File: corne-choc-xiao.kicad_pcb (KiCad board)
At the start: 2 copper layers, 111.3 x 87.7 mm, 51 parts, among them J1 LiPo, Q1 SI2032, SW10 SW_PUSH, SW11 SW_PUSH, SW12 SW_PUSH, SW14 SW_PUSH, SW15 SW_PUSH, SW16 SW_PUSH, SW17 SW_PUSH, SW18 SW_PUSH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

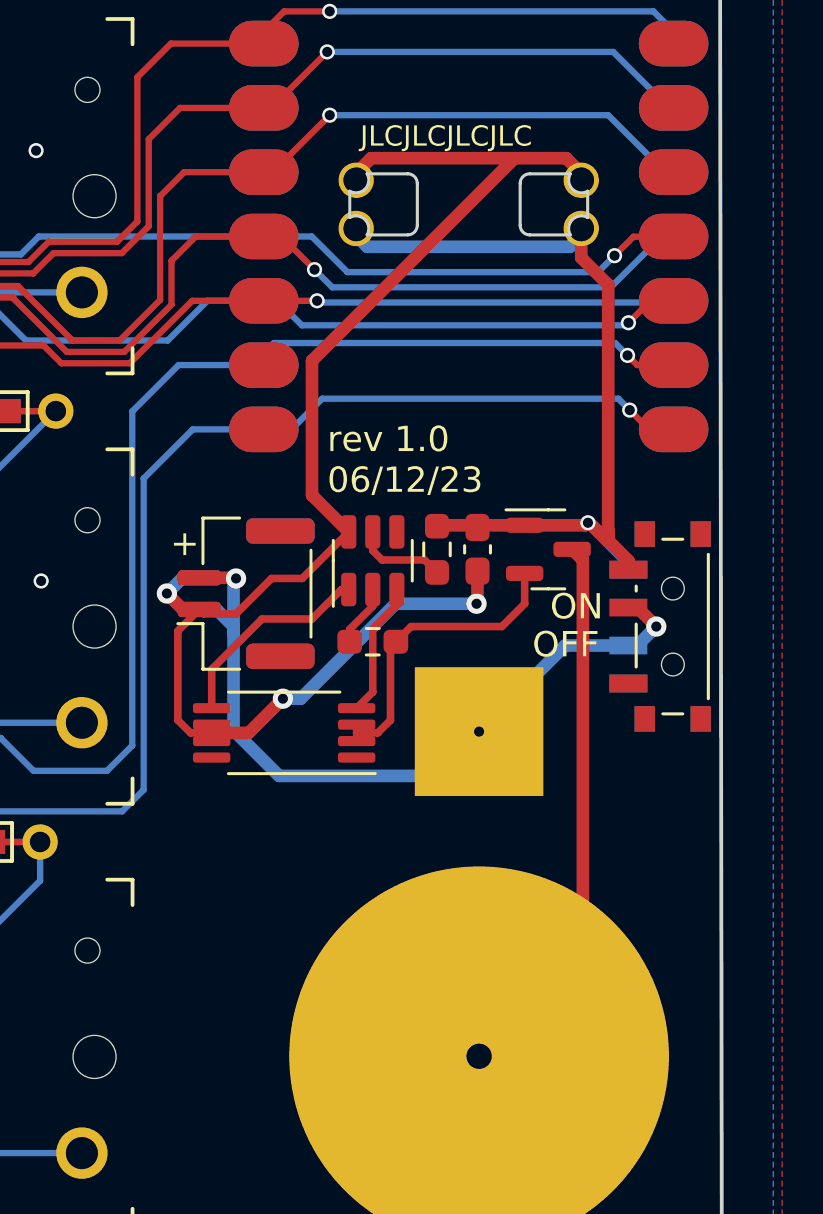
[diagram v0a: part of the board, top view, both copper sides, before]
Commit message: fix battery protection circuit
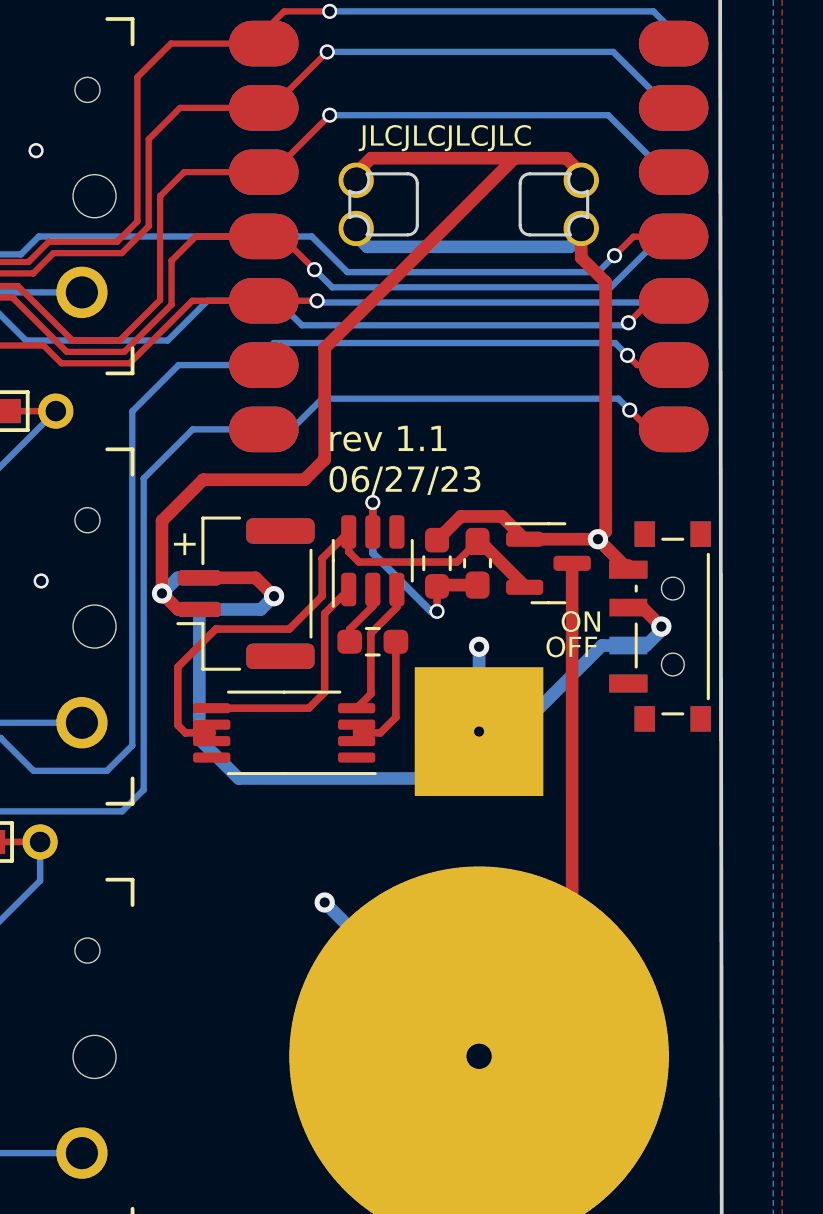
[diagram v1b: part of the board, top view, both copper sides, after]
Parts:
- BT1: value 3002 -> LIR2032
- Q1: value SI2032 -> SI2302
- R1: value 100R -> 330R
- R2: value 1k -> 2.7k
- moved C1 0.55 mm to (178.5, 75.9), turned to 90 degrees
- moved Q1 0.55 mm to (181.3, 75.9)
- moved R1 0.55 mm to (176.9, 75.9)
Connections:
- C1 pad 1: BAT+ -> Net-(U2-VCC)
- C1 pad 2: GND -> BAT-
- R2 pad 2: BAT- -> GND
- U2 pad 6: GND -> BAT-
- U3 pad 2: BAT- -> GND
- U3 pad 3: BAT- -> GND
- U3 pad 6: GND -> BAT-
- U3 pad 7: GND -> BAT-
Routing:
- net GND: track 59.8 -> 44.2 mm, vias 11 -> 9
- net Net-(Q1-D): track 21.9 -> 35.4 mm, vias 0 -> 1
- net BAT-: track 12.6 -> 23.4 mm
- net Net-(J1-Pin_2): track 32.1 -> 38.0 mm, vias 2 -> 3
- net Net-(U2-VCC): track 3.63 -> 9.38 mm, vias 0 -> 2
- net Net-(U2-OD): track 8.25 -> 9.18 mm
- net BAT+: track 34.2 -> 33.3 mm
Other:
- board text added: "rev 1.1 06/27/23"
- board text removed: "rev 1.0 06/12/23"

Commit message: added readme and ibom
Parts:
- R1: value 330R -> 100R
- R2: value 2.7k -> 1k
- renumbered SW22 to S1
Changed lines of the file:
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@@
   (title_block
     (title "corne-xiao")
-    (date "2023-06-12")
-    (rev "1.0")
+    (date "2023-06-27")
+    (rev "1.1")
   )
   (layers
@@
     (property "ki_keywords" "switch single-pole double-throw spdt ON-ON")
     (attr smd)
-    (fp_text reference "SW22" (at 8 5.2 90) (layer "F.Fab") hide
+    (fp_text reference "S1" (at 8 5.2 90) (layer "F.Fab") hide
         (effects (font (size 1 1) (thickness 0.15)))
     )
@@
         (effects (font (size 1 1) (thickness 0.15)))
     )
-    (fp_text value "2.7k" (at 0 1.43) (layer "F.Fab")
+    (fp_text value "1k" (at 0 1.43) (layer "F.Fab")
         (effects (font (size 1 1) (thickness 0.15)))
     )
@@
         (effects (font (size 1 1) (thickness 0.15)))
     )
-    (fp_text value "330R" (at 0 1.43 90) (layer "F.Fab")
+    (fp_text value "100R" (at 0 1.43 90) (layer "F.Fab")
         (effects (font (size 1 1) (thickness 0.15)))
     )

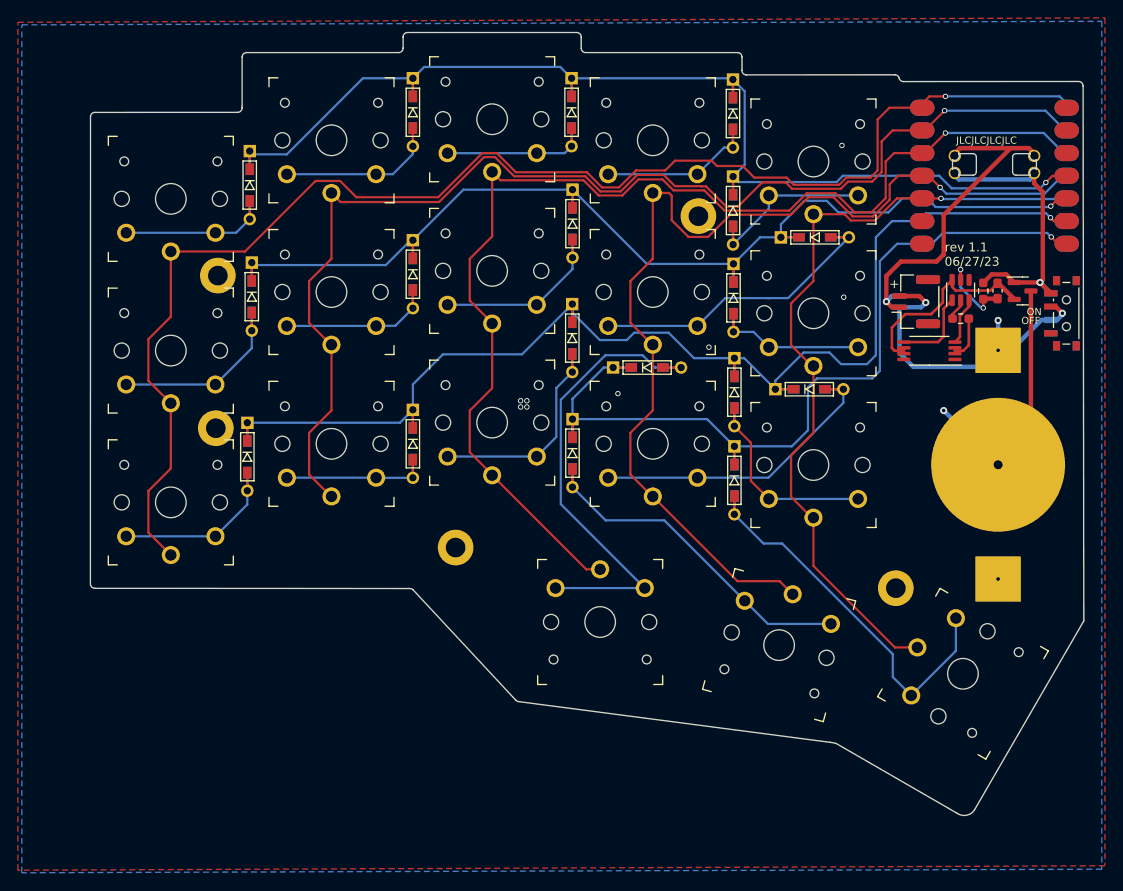
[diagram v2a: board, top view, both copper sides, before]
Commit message: added hotswap and removed lipo connector
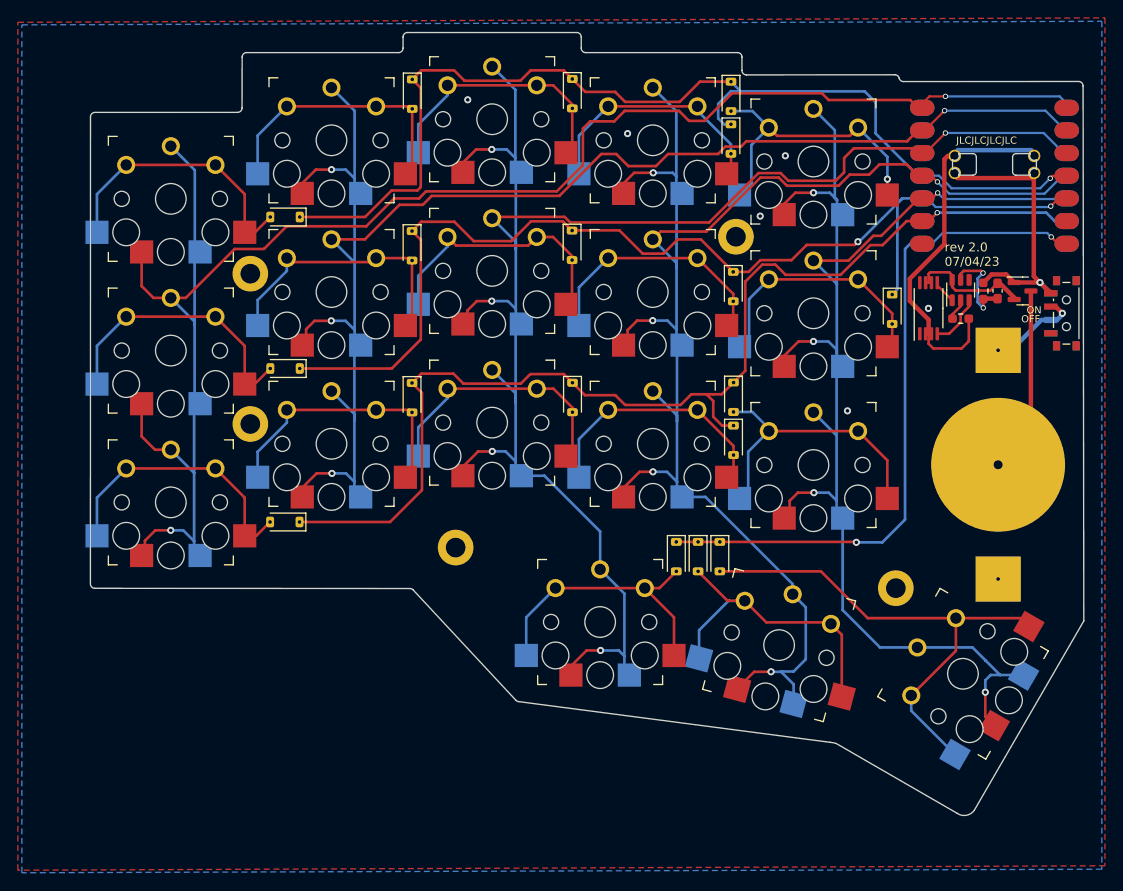
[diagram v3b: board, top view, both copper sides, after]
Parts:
- removed J1: LiPo, Connector_JST:JST_GH_SM02B-GHS-TB_1x02-1MP_P1.25mm_Horizontal
- D10, D11, D12, D14, D15, D16, D17, D18, D19, D2, D20, D21, D3, D4, D5, D6, D8, D9: footprint kbd:D3_TH_SMD -> corne-choc-xiao:SOD-123-TH
- SW10, SW11, SW12, SW14, SW15, SW16, SW17, SW18, SW19, SW2, SW20, SW3, SW4, SW5, SW6, SW8, SW9: footprint chocs:SW_PG1350_reversible_b2 -> corne-choc-xiao:Kailh_socket_PG1350_optional_reversible
- SW21: footprint Kailh:SW_PG1350_15_reversible_b2 -> corne-choc-xiao:Kailh_socket_PG1350_optional_reversible
- moved D19 21.4 mm to (142.5, 105.7), turned to -90 degrees
- moved D20 18.2 mm to (145.0, 105.7)
- moved D12 17.8 mm to (166.7, 78.0)
- moved D6 12.8 mm to (148.7, 54.1)
- moved D11 10.7 mm to (148.9, 75.4), turned to -90 degrees
- moved D17 10.3 mm to (148.9, 92.6), turned to -90 degrees
- moved D8 8.86 mm to (98.7, 84.6), turned to 180 degrees
- moved D21 8.70 mm to (147.4, 105.7)
- moved D14 8.42 mm to (98.7, 101.8), turned to 180 degrees
- moved D16 6.66 mm to (130.9, 87.8)
- moved D2 5.32 mm to (98.7, 67.6), turned to 180 degrees
- moved D15 5.17 mm to (112.9, 87.9)
- moved h2 4.80 mm to (149.2, 69.8)
- moved U3 4.77 mm to (170.8, 77.8), turned to 90 degrees
- moved h2 3.90 mm to (94.8, 90.8)
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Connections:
- U1 pad 9: row2 -> unconnected-(U1-A7_SCK/1.13-Pad9)
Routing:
- net col5: track 89.2 -> 153.7 mm, vias 1 -> 5
- net col3: track 131.5 -> 190.8 mm, vias 1 -> 5
- net col4: track 116.2 -> 173.0 mm, vias 1 -> 5
- net col1: track 157.0 -> 194.9 mm, vias 1 -> 2
- net col2: track 135.3 -> 171.4 mm, vias 1 -> 4
- net Net-(S1-B): track 38.0 -> 13.2 mm, vias 3 -> 1
- net row3: track 98.0 -> 76.9 mm, vias 1 -> 2
- net Net-(D19-A): track 53.1 -> 32.1 mm
- net row2: track 142.9 -> 125.9 mm
- net Net-(D2-A): track 18.5 -> 31.4 mm
- net Net-(D15-A): track 18.2 -> 30.6 mm
- net Net-(D6-A): track 21.4 -> 33.6 mm, vias 0 -> 1
- net Net-(D21-A): track 44.5 -> 56.6 mm
- net Net-(D9-A): track 19.0 -> 31.0 mm
- net row0: track 130.8 -> 119.0 mm
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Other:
- board text added: "rev 2.0 07/04/23"
- board text removed: "+"
- board text removed: "rev 1.1 06/27/23"
